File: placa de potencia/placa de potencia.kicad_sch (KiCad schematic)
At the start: 18 parts, among them J1 XT60-M, J10 B4B-XH-A, J11 B4B-XH-A, J12 B4B-XH-A, J13 B4B-XH-A, J2 XT60-M, J3 B4B-XH-A, J4 XT60-M, J5 B4B-XH-A, J6 B4B-XH-A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

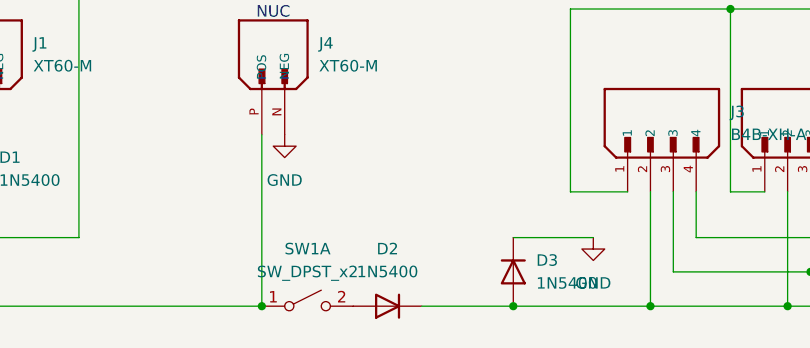
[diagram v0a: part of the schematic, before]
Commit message: Adionei o arduino na placa integrada (nao terminei) Adicionei a pasta de teclado (projeto pessoal)
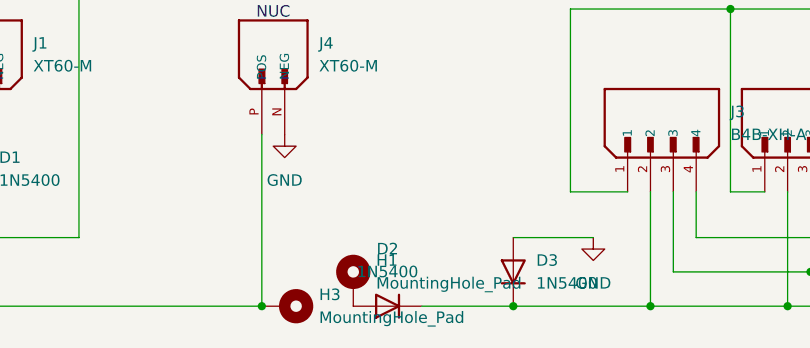
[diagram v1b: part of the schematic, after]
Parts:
- removed SW1: SW_DPST_x2, symbol Switch:SW_DPST_x2
- added H1, H3: MountingHole_Pad, MountingHole:MountingHole_2.5mm_Pad, symbol Mechanical:MountingHole_Pad
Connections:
- net GND: now also D3.2 (A); no longer D3.1 (K)
- net at D1.1 (K), D5.1 (K), J4.P (POS): now also H3.1
- net at D2.2 (A): now also H1.1
- net at D2.1 (K), J10.2, J11.2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: now also D3.1 (K); no longer D3.2 (A)
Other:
- moved on the sheet: D3
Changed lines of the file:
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@@
 	)
 	(junction
-		(at 81.28 57.15)
+		(at 262.89 24.13)
 		(diameter 0)
 		(color 0 0 0 0)
 	)
 	(junction
-		(at 262.89 24.13)
+		(at 246.38 24.13)
 		(diameter 0)
 		(color 0 0 0 0)
 	)
 	(junction
-		(at 246.38 24.13)
+		(at 238.76 53.34)
 		(diameter 0)
 		(color 0 0 0 0)
 	)
 	(junction
-		(at 238.76 53.34)
+		(at 109.22 57.15)
 		(diameter 0)
 		(color 0 0 0 0)
@@
 	)
 	(junction
+		(at 81.28 57.15)
+		(diameter 0)
+		(color 0 0 0 0)
+	)
+	(junction
 		(at 139.7 57.15)
 		(diameter 0)
@@
 		(color 0 0 0 0)
 	)
-	(junction
-		(at 109.22 57.15)
-		(diameter 0)
-		(color 0 0 0 0)
-	)
 	(wire
 		(pts
@@
 	(wire
 		(pts
-			(xy 81.28 38.1) (xy 81.28 57.15)
+			(xy 109.22 57.15) (xy 124.46 57.15)
 		)
 		(stroke
@@
 	(wire
 		(pts
-			(xy 109.22 57.15) (xy 124.46 57.15)
-		)
-		(stroke
-			(width 0)
-			(type default)
-		)
-	)
-	(wire
-		(pts
 			(xy 203.2 57.15) (xy 219.71 57.15)
 		)
@@
 		)
 	)
+	(wire
+		(pts
+			(xy 81.28 38.1) (xy 81.28 57.15)
+		)
+		(stroke
+			(width 0)
+			(type default)
+		)
+	)
 	(text "NUC\n"
 		(exclude_from_sim no)
@@
 	)
 	(symbol
-		(lib_id "Switch:SW_DPST_x2")
-		(at 86.36 57.15 0)
+		(lib_id "Mechanical:MountingHole_Pad")
+		(at 83.82 57.15 270)
 		(unit 1)
-		(exclude_from_sim no)
-		(in_bom yes)
+		(exclude_from_sim yes)
+		(in_bom no)
 		(on_board yes)
 		(dnp no)
 		(fields_autoplaced yes)
-		(property "Reference" "SW1"
-			(at 86.36 50.8 0)
+		(property "Reference" "H3"
+			(at 87.63 55.8799 90)
 			(effects
 				(font
 					(size 1.27 1.27)
 				)
+				(justify left)
 			)
 		)
-		(property "Value" "SW_DPST_x2"
-			(at 86.36 53.34 0)
+		(property "Value" "MountingHole_Pad"
+			(at 87.63 58.4199 90)
 			(effects
 				(font
 					(size 1.27 1.27)
 				)
+				(justify left)
 			)
 		)
-		(property "Footprint" ""
-			(at 86.36 57.15 0)
+		(property "Footprint" "MountingHole:MountingHole_2.5mm_Pad"
+			(at 83.82 57.15 0)
 			(effects
 				(font
@@
 		)
 		(property "Datasheet" "~"
-			(at 86.36 57.15 0)
+			(at 83.82 57.15 0)
 			(effects
 				(font
@@
 			)
 		)
-		(property "Description" "Single Pole Single Throw (SPST) switch, separate symbol"
-			(at 86.36 57.15 0)
+		(property "Description" "Mounting Hole with connection"
+			(at 83.82 57.15 0)
 			(effects
 				(font
@@
 			)
 		)
-		(pin "2"
-		)
-		(pin "4"
-		)
-		(pin "3"
-		)
 		(pin "1"
 		)
@@
 			(project ""
 				(path "/e3dae42a-1d97-46f0-98f1-701c272a6f88"
-					(reference "SW1")
+					(reference "H3")
 					(unit 1)
 				)
@@
 	(symbol
 		(lib_id "Diode:1N5400")
-		(at 109.22 53.34 270)
+		(at 109.22 53.34 90)
 		(unit 1)
 		(exclude_from_sim no)
@@
 					(size 1.27 1.27)
 				)
-				(justify left)
+				(justify right)
 			)
 		)
@@
 					(size 1.27 1.27)
 				)
-				(justify left)
+				(justify right)
 			)
 		)
 		(property "Footprint" "Diode_THT:D_DO-201AD_P15.24mm_Horizontal"
-			(at 104.775 53.34 0)
+			(at 113.665 53.34 0)
 			(effects
 				(font
@@
 					(unit 1)
 				)
+			)
+		)
+	)
+	(symbol
+		(lib_id "Mechanical:MountingHole_Pad")
+		(at 91.44 54.61 0)
+		(unit 1)
+		(exclude_from_sim yes)
+		(in_bom no)
+		(on_board yes)
+		(dnp no)
+		(fields_autoplaced yes)
+		(property "Reference" "H1"
+			(at 93.98 52.0699 0)
+			(effects
+				(font
+					(size 1.27 1.27)
+				)
+				(justify left)
+			)
+		)
+		(property "Value" "MountingHole_Pad"
+			(at 93.98 54.6099 0)
+			(effects
+				(font
+					(size 1.27 1.27)
+				)
+				(justify left)
+			)
+		)
+		(property "Footprint" "MountingHole:MountingHole_2.5mm_Pad"
+			(at 91.44 54.61 0)
+			(effects
+				(font
+					(size 1.27 1.27)
+				)
+				(hide yes)
+			)
+		)
+		(property "Datasheet" "~"
+			(at 91.44 54.61 0)
+			(effects
+				(font
+					(size 1.27 1.27)
+				)
+				(hide yes)
+			)
+		)
+		(property "Description" "Mounting Hole with connection"
+			(at 91.44 54.61 0)
+			(effects
+				(font
+					(size 1.27 1.27)
+				)
+				(hide yes)
+			)
+		)
+		(pin "1"
+		)
+		(instances
+			(project ""
+				(path "/e3dae42a-1d97-46f0-98f1-701c272a6f88"
+					(reference "H1")
+					(unit 1)
+				)
